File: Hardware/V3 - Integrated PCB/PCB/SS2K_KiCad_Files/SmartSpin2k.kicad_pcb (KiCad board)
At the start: 2 copper layers, 57.2 x 60.3 mm, 84 parts, among them J1 B4B-XH-AMLFSN, J2 B4B-XH-AMLFSN, J3 B8B-XH-A_LFSN, J4 10118194-0001LF, Q1 S8050, Q2 S8050, SW1 SW_Push, SW2 SW_Push, U1 ESP32-WROOM-32D, U2 TMC2209-LA-T, U3 MAX3232, U4 TPS5430DDA, U5 INTERFACE-CP2102-GMR(QFN28), U6 LM1117-3.3

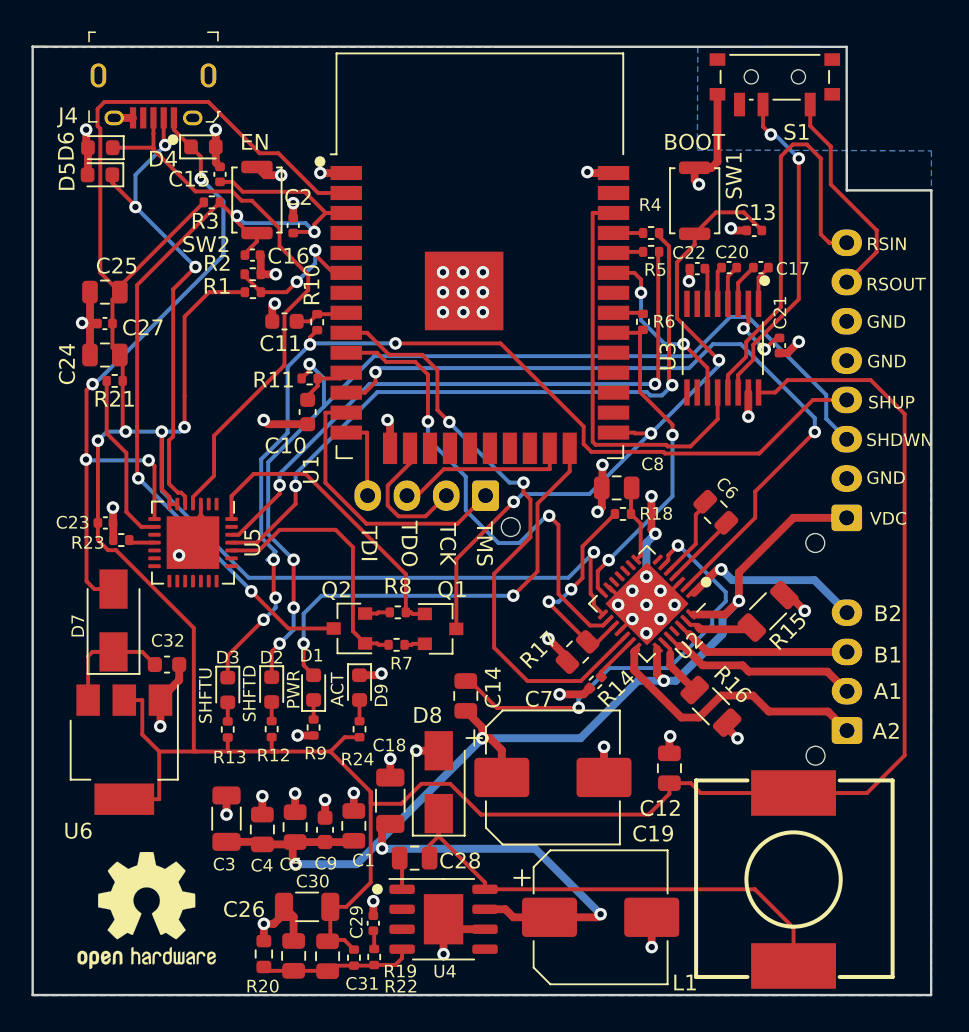
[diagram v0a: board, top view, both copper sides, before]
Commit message: New Board Changes to Switch and Edges
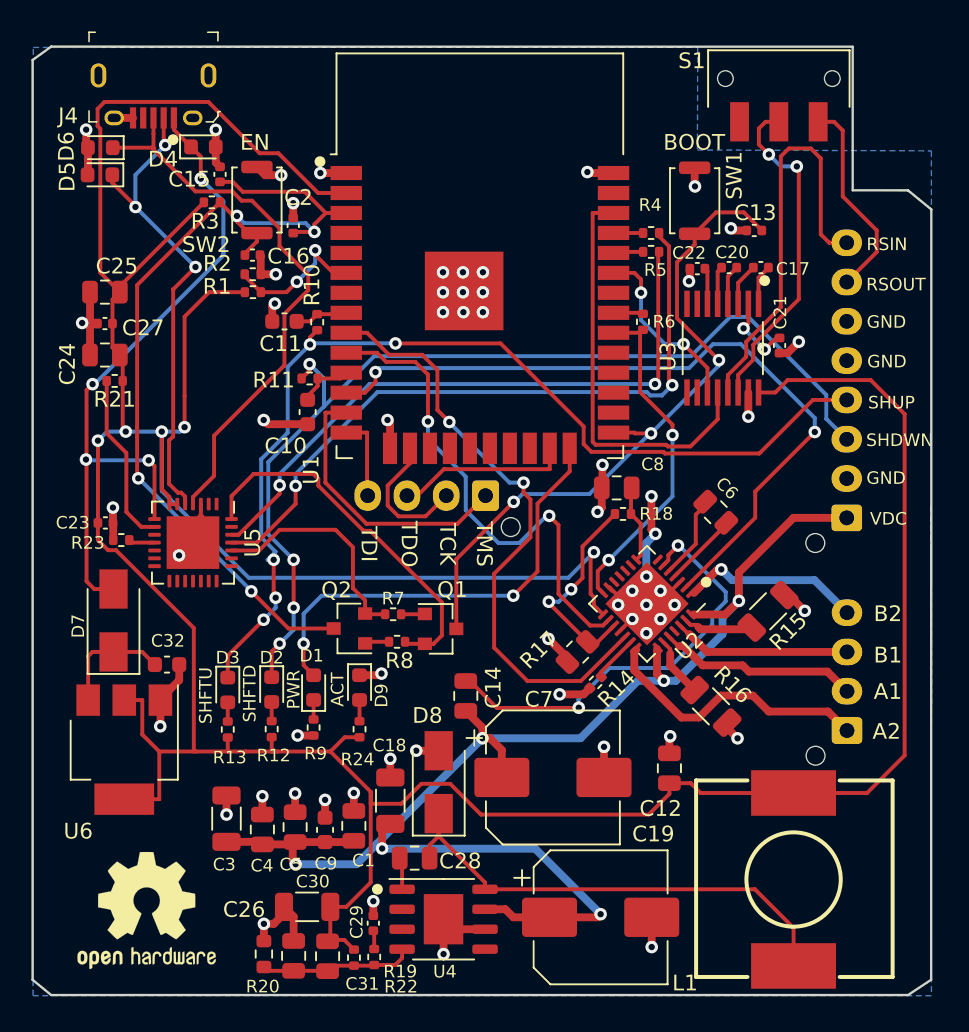
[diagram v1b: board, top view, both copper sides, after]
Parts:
- S1: value EG1218 -> JS102011SAQN; footprint Button_Switch_SMD:SW_SPDT_PCM12 -> Switch:SW_JS102011SAQN
- moved R7 1.96 mm to (144.2, 124.8)
- moved R8 1.87 mm to (144.5, 126.5)
- moved S1 0.34 mm to (168.8, 90.7)
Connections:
- Q1 pad 1: /DTR -> Net-(Q1-Pad1)
- Q1 pad 2: Net-(Q1-Pad2) -> /DTR
- Q2 pad 1: /RTS -> Net-(Q2-Pad1)
- Q2 pad 2: Net-(Q2-Pad2) -> /RTS
- R7 pad 1: Net-(Q1-Pad2) -> Net-(Q1-Pad1)
- R8 pad 2: Net-(Q2-Pad2) -> Net-(Q2-Pad1)
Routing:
- net GND: track 96.4 -> 90.5 mm
- net /DTR: track 19.5 -> 23.8 mm
- net /RTS: track 16.7 -> 14.6 mm
- net Net-(Q2-Pad2): track 1.60 -> 0.00 mm
- net Net-(Q2-Pad1): track 0.00 -> 1.56 mm
- net Net-(Q1-Pad1): track 0.00 -> 1.52 mm
- net Net-(Q1-Pad2): track 1.32 -> 0.00 mm
- net /RS232OUT1: track 13.8 -> 13.1 mm
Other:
- outline, holes or cut-outs redrawn
